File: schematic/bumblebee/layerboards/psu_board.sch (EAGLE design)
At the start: 49 parts, among them P1 B3B-EH-A, Q1 IRF9530, Q10 IRF9530, Q2 IRF9530, Q3 IRF9530, Q5 IRF9530, Q7 IRF9530, T1 2N7002E, T2 2N7002E, T3 2N7002E, T4 2N7002E, T5 2N7002E, T6 2N7002E

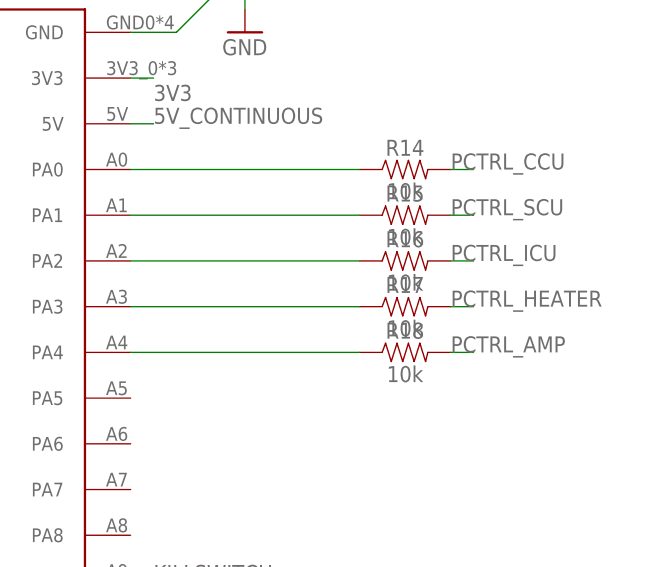
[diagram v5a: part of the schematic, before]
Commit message: Все платы готовы и отправлены в резонит
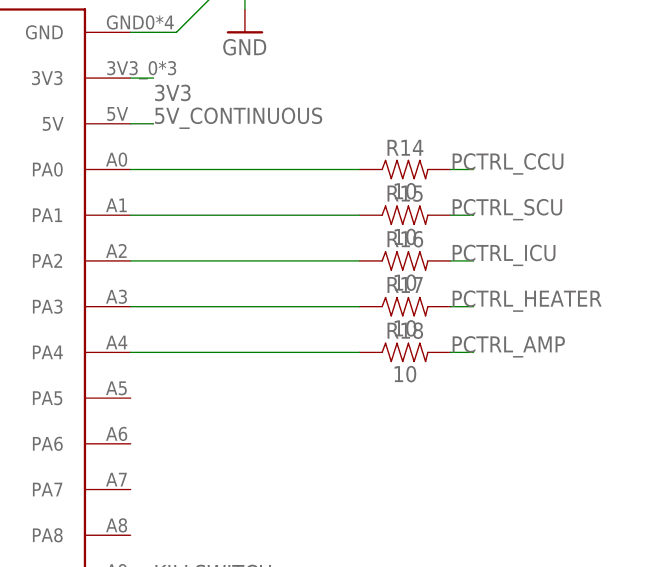
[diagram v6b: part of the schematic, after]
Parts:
- R14, R15, R16, R17, R18: value 10k -> 10
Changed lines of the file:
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@@
 <part name="R12" library="SparkFun-Resistors" deviceset="RESISTOR" device="AXIAL-0.3" value="10k"/>
 <part name="R13" library="SparkFun-Resistors" deviceset="RESISTOR" device="AXIAL-0.3" value="10k"/>
-<part name="R14" library="SparkFun-Resistors" deviceset="RESISTOR" device="AXIAL-0.3" value="10k"/>
-<part name="R15" library="SparkFun-Resistors" deviceset="RESISTOR" device="AXIAL-0.3" value="10k"/>
-<part name="R16" library="SparkFun-Resistors" deviceset="RESISTOR" device="AXIAL-0.3" value="10k"/>
-<part name="R17" library="SparkFun-Resistors" deviceset="RESISTOR" device="AXIAL-0.3" value="10k"/>
-<part name="R18" library="SparkFun-Resistors" deviceset="RESISTOR" device="AXIAL-0.3" value="10k"/>
+<part name="R14" library="SparkFun-Resistors" deviceset="RESISTOR" device="AXIAL-0.3" value="10"/>
+<part name="R15" library="SparkFun-Resistors" deviceset="RESISTOR" device="AXIAL-0.3" value="10"/>
+<part name="R16" library="SparkFun-Resistors" deviceset="RESISTOR" device="AXIAL-0.3" value="10"/>
+<part name="R17" library="SparkFun-Resistors" deviceset="RESISTOR" device="AXIAL-0.3" value="10"/>
+<part name="R18" library="SparkFun-Resistors" deviceset="RESISTOR" device="AXIAL-0.3" value="10"/>
 <part name="HEATER_7.4V" library="pinhead" library_urn="urn:adsk.eagle:library:325" deviceset="PINHD-1X1" device="" package3d_urn="urn:adsk.eagle:package:22485/2"/>
 <part name="HEATER_GND" library="pinhead" library_urn="urn:adsk.eagle:library:325" deviceset="PINHD-1X1" device="" package3d_urn="urn:adsk.eagle:package:22485/2"/>
